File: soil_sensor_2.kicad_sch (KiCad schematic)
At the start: 20 parts, among them J1 ESP-PROG, Q1 SI2312, U1 HDC1080, U2 TPS61201DRCT, U3 ESP32-PICO-V3

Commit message: update BMS
now using the TPS61201DRCT
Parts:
- removed U1: HDC1080, Package_SON:Texas_PWSON-N6, symbol soil_sensor_2-rescue:HDC1080-Sensor_Humidity
- added D1: LED, LED_SMD:LED_0603_1608Metric, symbol Device:LED
- added R4: 3k3, Resistor_SMD:R_0603_1608Metric, symbol Device:R_Small
- added U1: SHT40, Sensor_Humidity:Sensirion_DFN-4-1EP_2x2mm_P1mm_EP0.7x1.6mm, symbol Sensor_Humidity:SHTC1
- R1: value 2.87M -> 1M5
- renumbered C7 to C6, C6 to C7
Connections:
- net +3V3: now also U1.4 (VSS)
- net GND: now also R4.2, U1.1 (VDD)
- net RXD: now also U3.40 (U0RXD/GPIO3); no longer U3.41 (U0TXD/GPIO1)
- net SCL: now also U1.2 (SCL)
- net SDA: now also U1.3 (SDA)
- net TXD: now also U3.41 (U0TXD/GPIO1); no longer U3.40 (U0RXD/GPIO3)
- net at U3.38 (GPIO19): now also D1.2 (A)
- new net: D1.1 (K), R4.1
- no-connect marks 23 -> 22
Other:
- note added: "2.9V cutoff"
- note removed: "2.9V cutoff for LiFePO4"
- moved on the sheet: C2, C6, R3

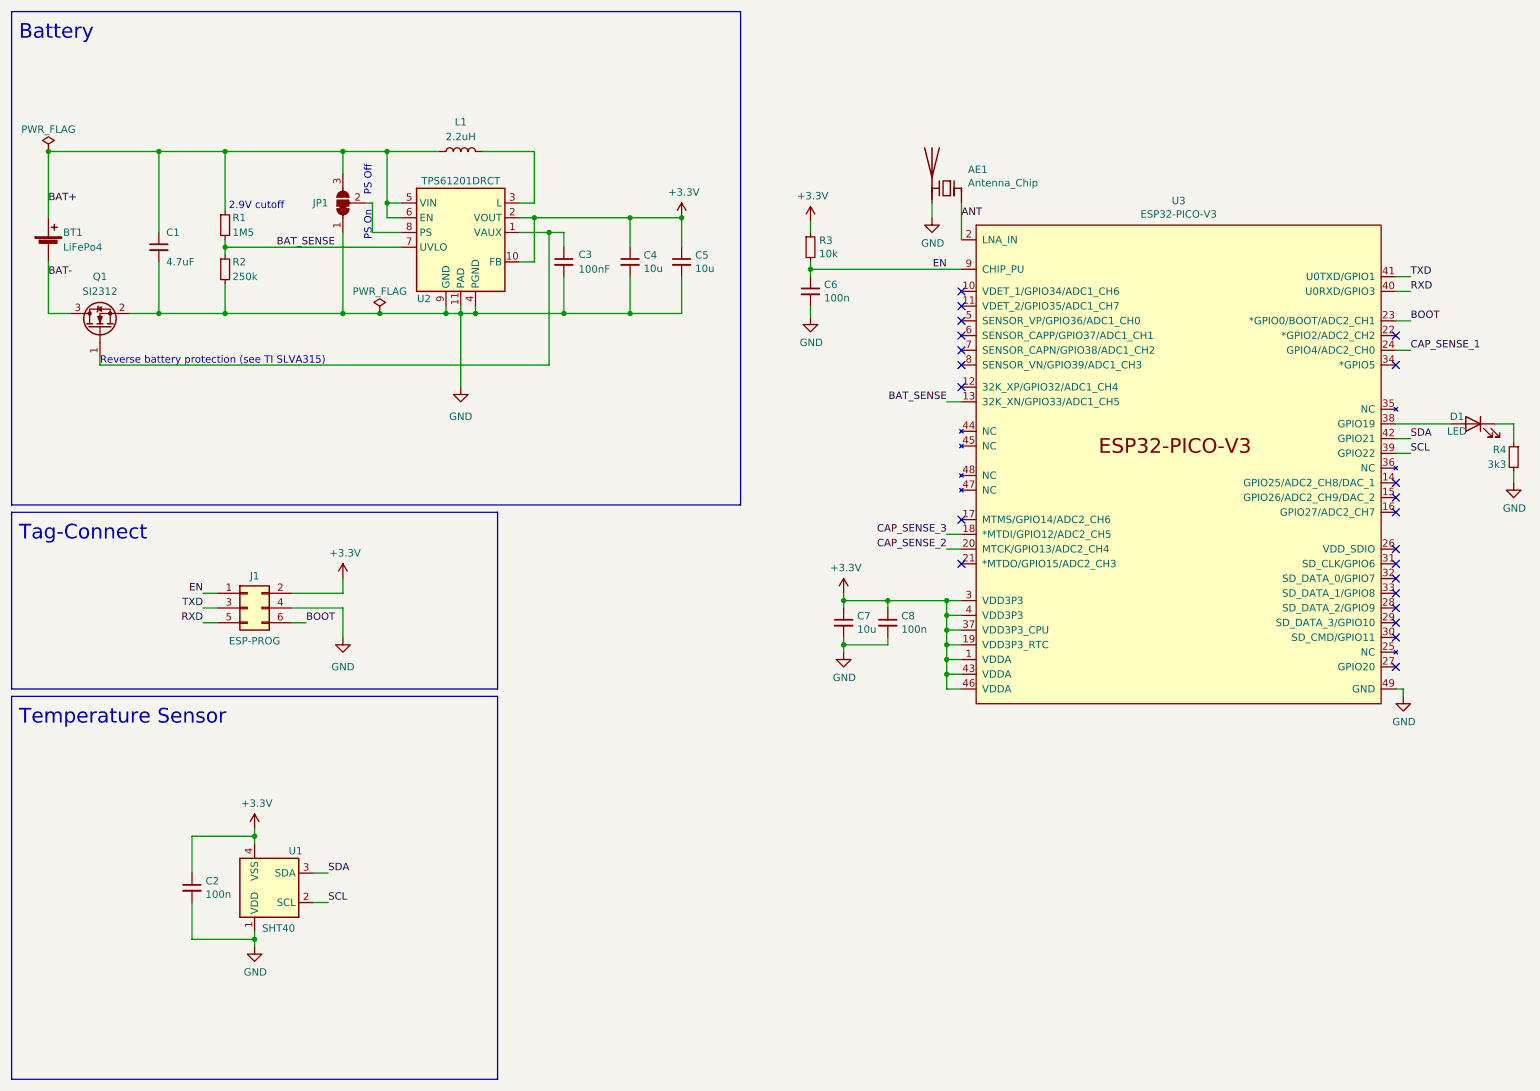
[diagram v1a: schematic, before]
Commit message: added some comments
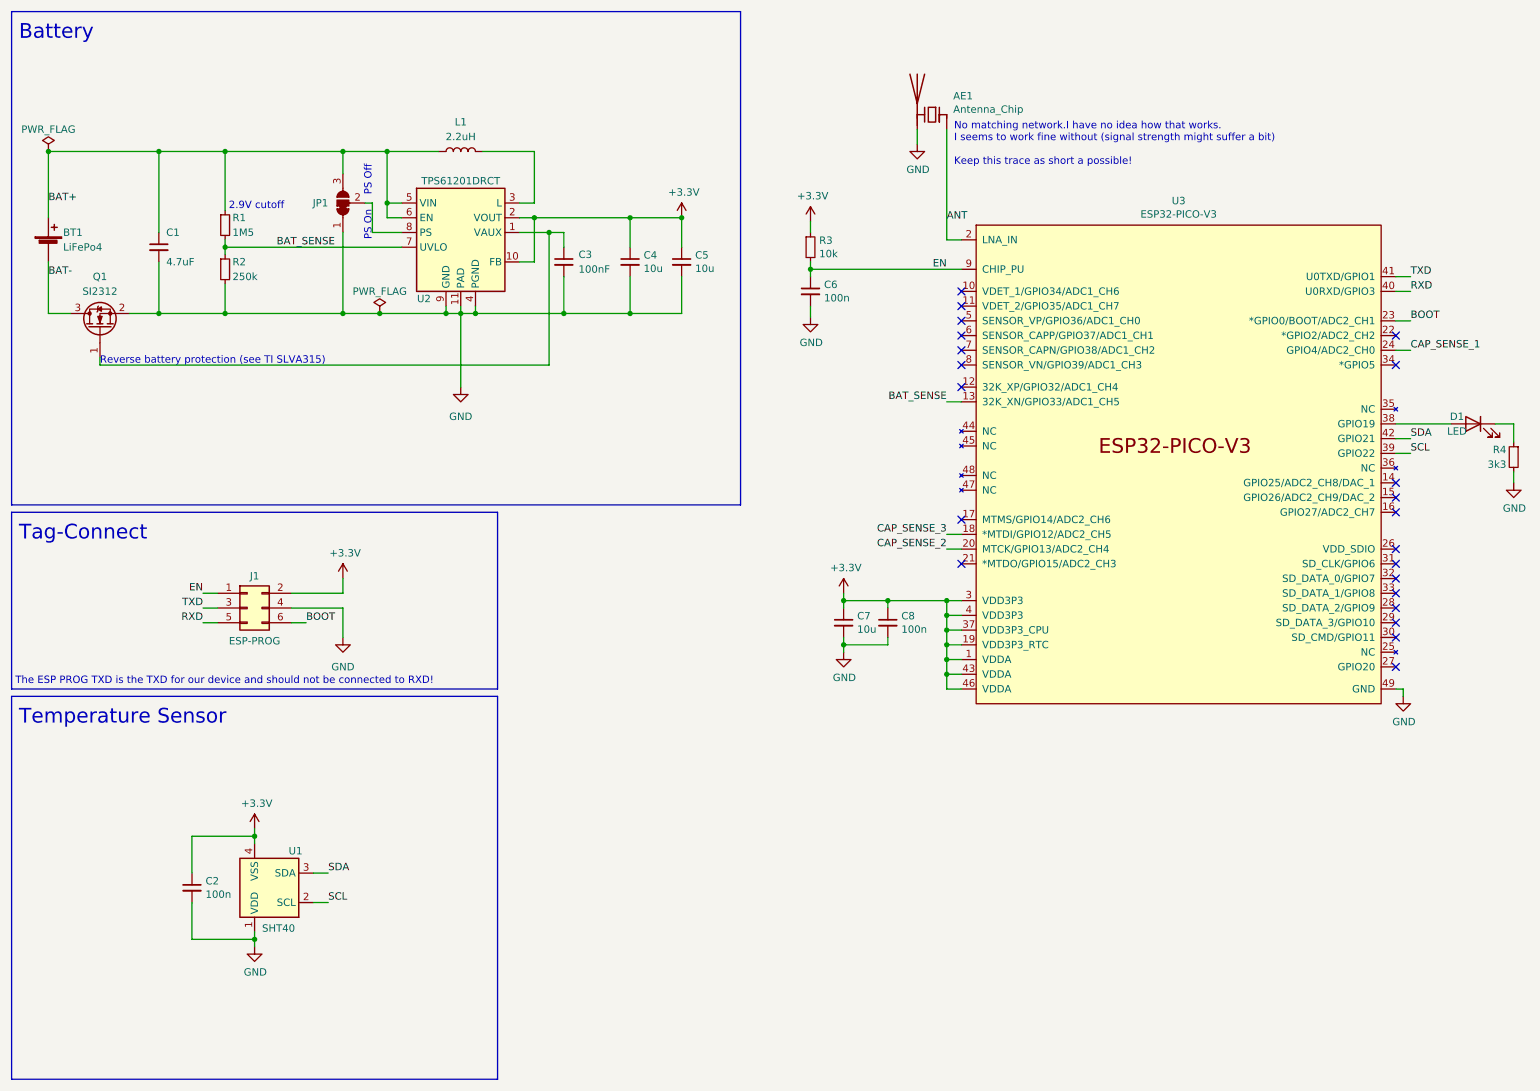
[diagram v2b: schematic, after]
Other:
- note added: "No matching network.I have no idea how that works. I seems to work fine without (signal strength might suffer a bit) Keep this trace as short a possible!"
- note added: "The ESP PROG TXD is the TXD for our device and should not be connected to RXD!"
- moved on the sheet: AE1
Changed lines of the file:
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@@
+    (stroke (width 0) (type default) (color 0 0 0 0))
+  )
+  (wire (pts (xy 173.99 33.02) (xy 173.99 52.07))
     (stroke (width 0) (type default) (color 0 0 0 0))
   )
@@
     (stroke (width 0) (type default) (color 0 0 0 0))
   )
+  (wire (pts (xy 173.99 52.07) (xy 176.53 52.07))
+    (stroke (width 0) (type default) (color 0 0 0 0))
+  )
   (wire (pts (xy 251.46 58.42) (xy 254 58.42))
     (stroke (width 0) (type solid) (color 0 0 0 0))
@@
     (stroke (width 0) (type solid) (color 0 0 0 0))
   )
-  (wire (pts (xy 171.45 45.72) (xy 171.45 48.26))
+  (wire (pts (xy 168.91 33.02) (xy 168.91 35.56))
     (stroke (width 0) (type solid) (color 0 0 0 0))
   )
@@
   (wire (pts (xy 38.1 64.77) (xy 49.53 64.77))
     (stroke (width 0) (type default) (color 0 0 0 0))
-  )
-  (wire (pts (xy 176.53 45.72) (xy 176.53 52.07))
-    (stroke (width 0) (type solid) (color 0 0 0 0))
   )
   (wire (pts (xy 77.47 48.26) (xy 77.47 45.72))
@@
     (effects (font (size 2.54 2.54)) (justify left bottom))
   )
+  (text "The ESP PROG TXD is the TXD for our device and should not be connected to RXD!"
+    (at 13.335 128.905 0)
+    (effects (font (size 1.27 1.27)) (justify left bottom))
+  )
   (text "PS Off" (at 74.93 44.45 90)
     (effects (font (size 1.27 1.27)) (justify left bottom))
@@
     (effects (font (size 1.27 1.27)) (justify left bottom))
   )
+  (text "No matching network.I have no idea how that works.\nI seems to work fine without (signal strength might suffer a bit)\n\nKeep this trace as short a possible!"
+    (at 175.26 39.37 0)
+    (effects (font (size 1.27 1.27)) (justify left bottom))
+  )
   (label "EN" (at 173.99 57.15 180)
     (effects (font (size 1.27 1.27)) (justify right bottom))
@@
     (effects (font (size 1.27 1.27)) (justify left bottom))
   )
-  (label "ANT" (at 176.53 48.26 0)
+  (label "ANT" (at 173.99 48.895 0)
     (effects (font (size 1.27 1.27)) (justify left bottom))
   )
@@
     (pin "1")
   )
-  (symbol (lib_id "soil_sensor_2-rescue:Antenna_Chip-Device") (at 173.99 43.18 0) (mirror y) (unit 1)
-    (in_bom yes) (on_board yes)
-    (property "Reference" "AE1" (id 0) (at 177.6476 39.9542 0)
+  (symbol (lib_id "soil_sensor_2-rescue:Antenna_Chip-Device") (at 171.45 30.48 0) (mirror y) (unit 1)
+    (in_bom yes) (on_board yes)
+    (property "Reference" "AE1" (id 0) (at 175.1076 27.2542 0)
       (effects (font (size 1.27 1.27)) (justify right))
     )
-    (property "Value" "Antenna_Chip" (id 1) (at 177.6476 42.2656 0)
+    (property "Value" "Antenna_Chip" (id 1) (at 175.1076 29.5656 0)
       (effects (font (size 1.27 1.27)) (justify right))
     )
-    (property "Footprint" "RF_Antenna:Texas_SWRA117D_2.4GHz_Right" (id 2) (at 176.53 38.735 0)
-      (effects (font (size 1.27 1.27)) hide)
-    )
-    (property "Datasheet" "~" (id 3) (at 176.53 38.735 0)
+    (property "Footprint" "RF_Antenna:Texas_SWRA117D_2.4GHz_Right" (id 2) (at 173.99 26.035 0)
+      (effects (font (size 1.27 1.27)) hide)
+    )
+    (property "Datasheet" "~" (id 3) (at 173.99 26.035 0)
       (effects (font (size 1.27 1.27)) hide)
     )
@@
     (pin "2")
   )
-  (symbol (lib_id "soil_sensor_2-rescue:GND-power") (at 171.45 48.26 0) (unit 1)
-    (in_bom yes) (on_board yes)
-    (property "Reference" "#PWR011" (id 0) (at 171.45 54.61 0)
-      (effects (font (size 1.27 1.27)) hide)
-    )
-    (property "Value" "GND" (id 1) (at 171.577 52.6542 0))
-    (property "Footprint" "" (id 2) (at 171.45 48.26 0)
-      (effects (font (size 1.27 1.27)) hide)
-    )
-    (property "Datasheet" "" (id 3) (at 171.45 48.26 0)
-      (effects (font (size 1.27 1.27)) hide)
-    )
+  (symbol (lib_id "soil_sensor_2-rescue:GND-power") (at 168.91 35.56 0) (unit 1)
+    (in_bom yes) (on_board yes)
+    (property "Reference" "#PWR011" (id 0) (at 168.91 41.91 0)
+      (effects (font (size 1.27 1.27)) hide)
+    )
+    (property "Value" "GND" (id 1) (at 169.037 39.9542 0))
+    (property "Footprint" "" (id 2) (at 168.91 35.56 0)
+      (effects (font (size 1.27 1.27)) hide)
+    )
+    (property "Datasheet" "" (id 3) (at 168.91 35.56 0)
+      (effects (font (size 1.27 1.27)) hide)
+    )

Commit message: move battery off pcb
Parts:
- removed BT1: LiFePo4, Soil_Sensor:BatteryHolder_Keystone_2460_1xAA, symbol Device:Battery_Cell
- removed JP1: SolderJumper_3_Bridged12, Jumper:SolderJumper-3_P1.3mm_Bridged12_RoundedPad1.0x1.5mm, symbol Jumper:SolderJumper_3_Bridged12
- removed U1: SHT40, Sensor_Humidity:Sensirion_DFN-4-1EP_2x2mm_P1mm_EP0.7x1.6mm, symbol Sensor_Humidity:SHTC1
- added J1: 532610471, MOLEX_532610471, symbol Molex_picoblade:532610471
- added U1: SHT4x, Soil_Sensor:XDCR_SHT40-AD1B-R2, symbol Soil_Sensor:SHT4x
- renumbered C2 to C1, C1 to C2, J1 to J2
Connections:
- net +3V3: now also U1.3 (VDD)
- net BAT+: now also J1.4
- net BAT-: now also J1.1
- net GND: now also U2.8 (PS), J1.S1 (SHIELD1), J1.S2 (SHIELD2), U1.4 (VSS)
- net SDA_{1}: now reaches U3.28 (SD_DATA_2/GPIO9)
- net SDA_{1}: now also J1.3
- net SCL_{1}: now reaches U3.29 (SD_DATA_3/GPIO10)
- net SCL_{1}: now also J1.2
- net SCL renamed SDA_{0}
- net SDA_{0}: now also U1.1 (SDA)
- net SDA renamed SCL_{0}
- net SCL_{0}: now also U1.2 (SCL)
- no-connect marks 22 -> 20
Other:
- note removed: "PS Off"
- note removed: "PS On"
- moved on the sheet: C2, C3, C4, C5, L1, Q1, R1, R2, U2
